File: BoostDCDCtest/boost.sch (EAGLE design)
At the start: 28 parts, among them IC1 SI8235-IS1, M1 FET_ON_SOCKET

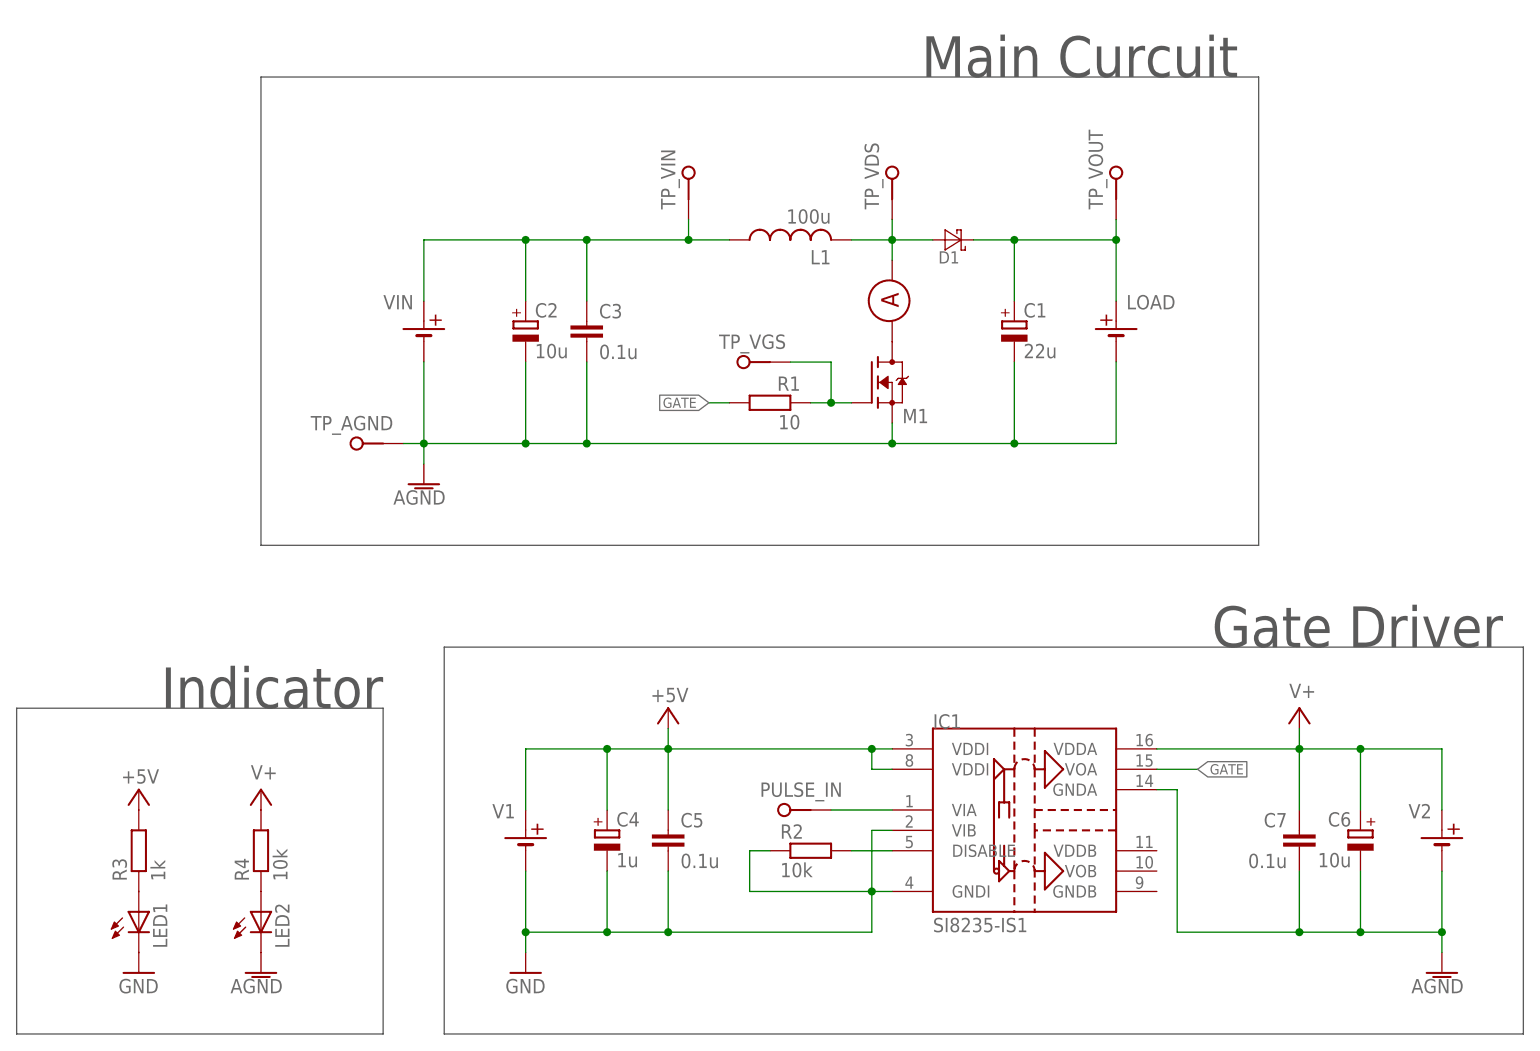
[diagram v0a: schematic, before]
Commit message: 1st brd completed
sch has been also editted because there is some issues of tolerance in the test situation.
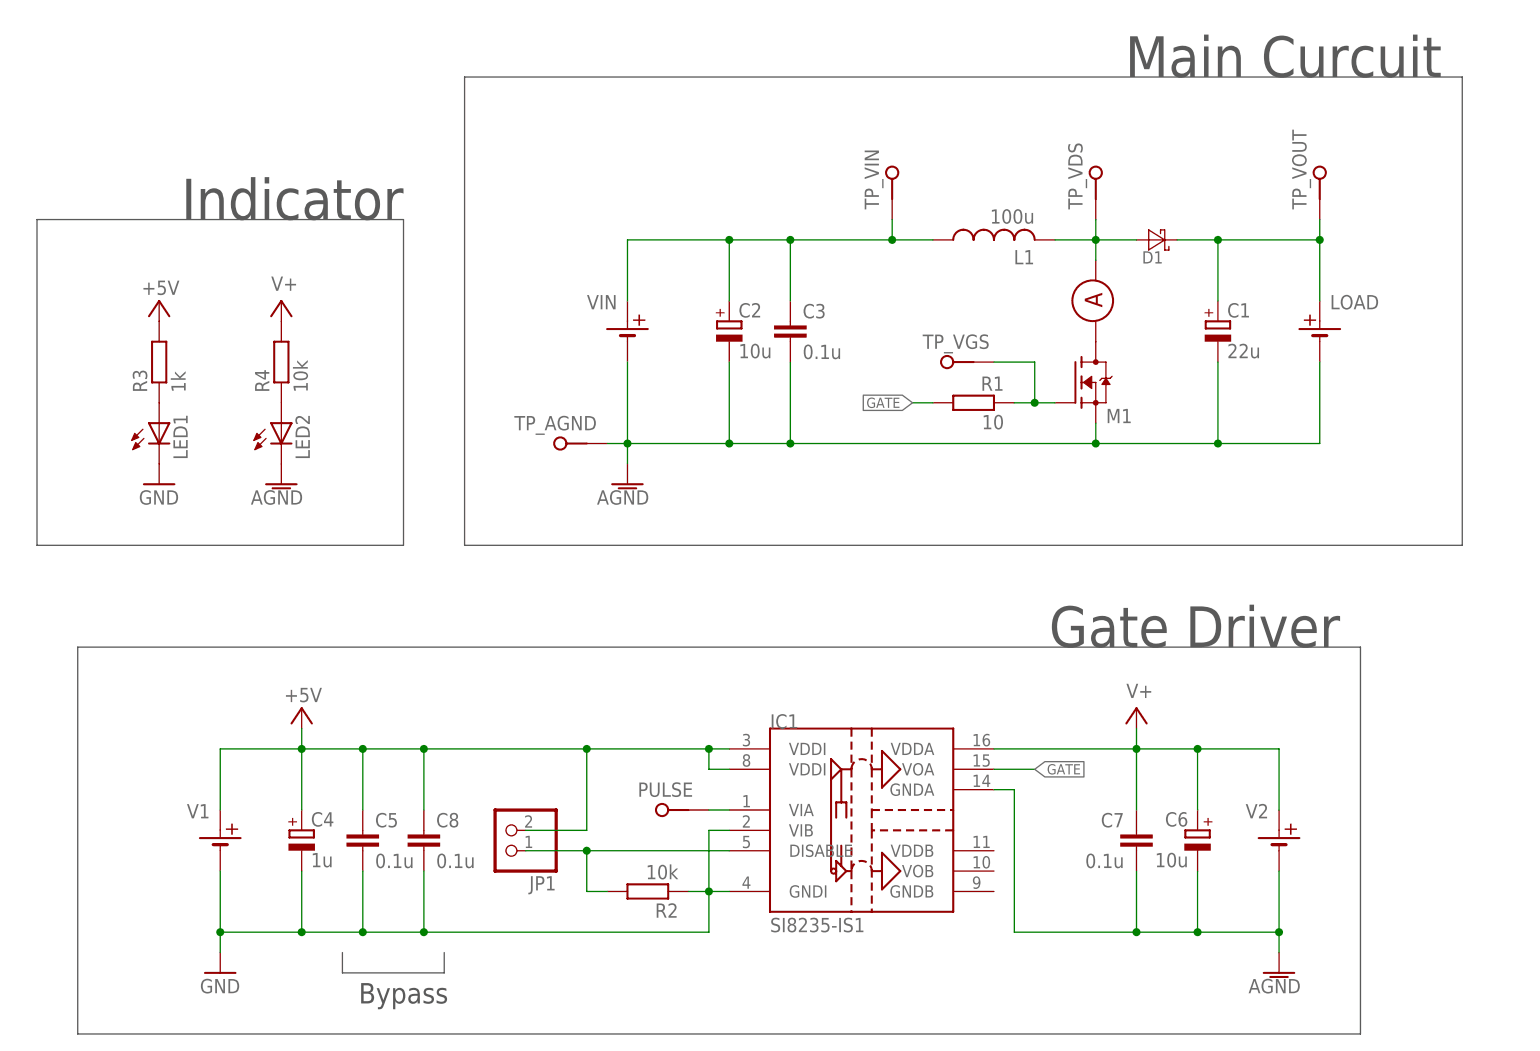
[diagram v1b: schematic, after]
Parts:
- removed PULSE_IN: PIN, lab:PIN
- added C8: 0.1u, resistor:C-EUC0805
- added JP1: (no value), pinhead:PINHD-1X2
- added PULSE: PIN, lab:PIN
- C5: device rcl:C-EUC0805K -> resistor:C-EUC0805
- R1: device resistor:R-EU_R0805 -> resistor:R-EU_R2512
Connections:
- net +5V: now also C8.1, JP1.2
- net GND: now also C8.2
- net N$5: now also JP1.1
- net N$6: now also PULSE.KL; no longer PULSE_IN.KL
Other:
- note added: "Bypass"
- moved on the sheet: C1, C2, C3, C4, C5, C6, C7, D1, IC1, L1, LED1, LED2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
